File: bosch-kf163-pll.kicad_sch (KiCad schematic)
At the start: 7 parts, among them J101 TGA, U101 ESP32-WROOM-32U

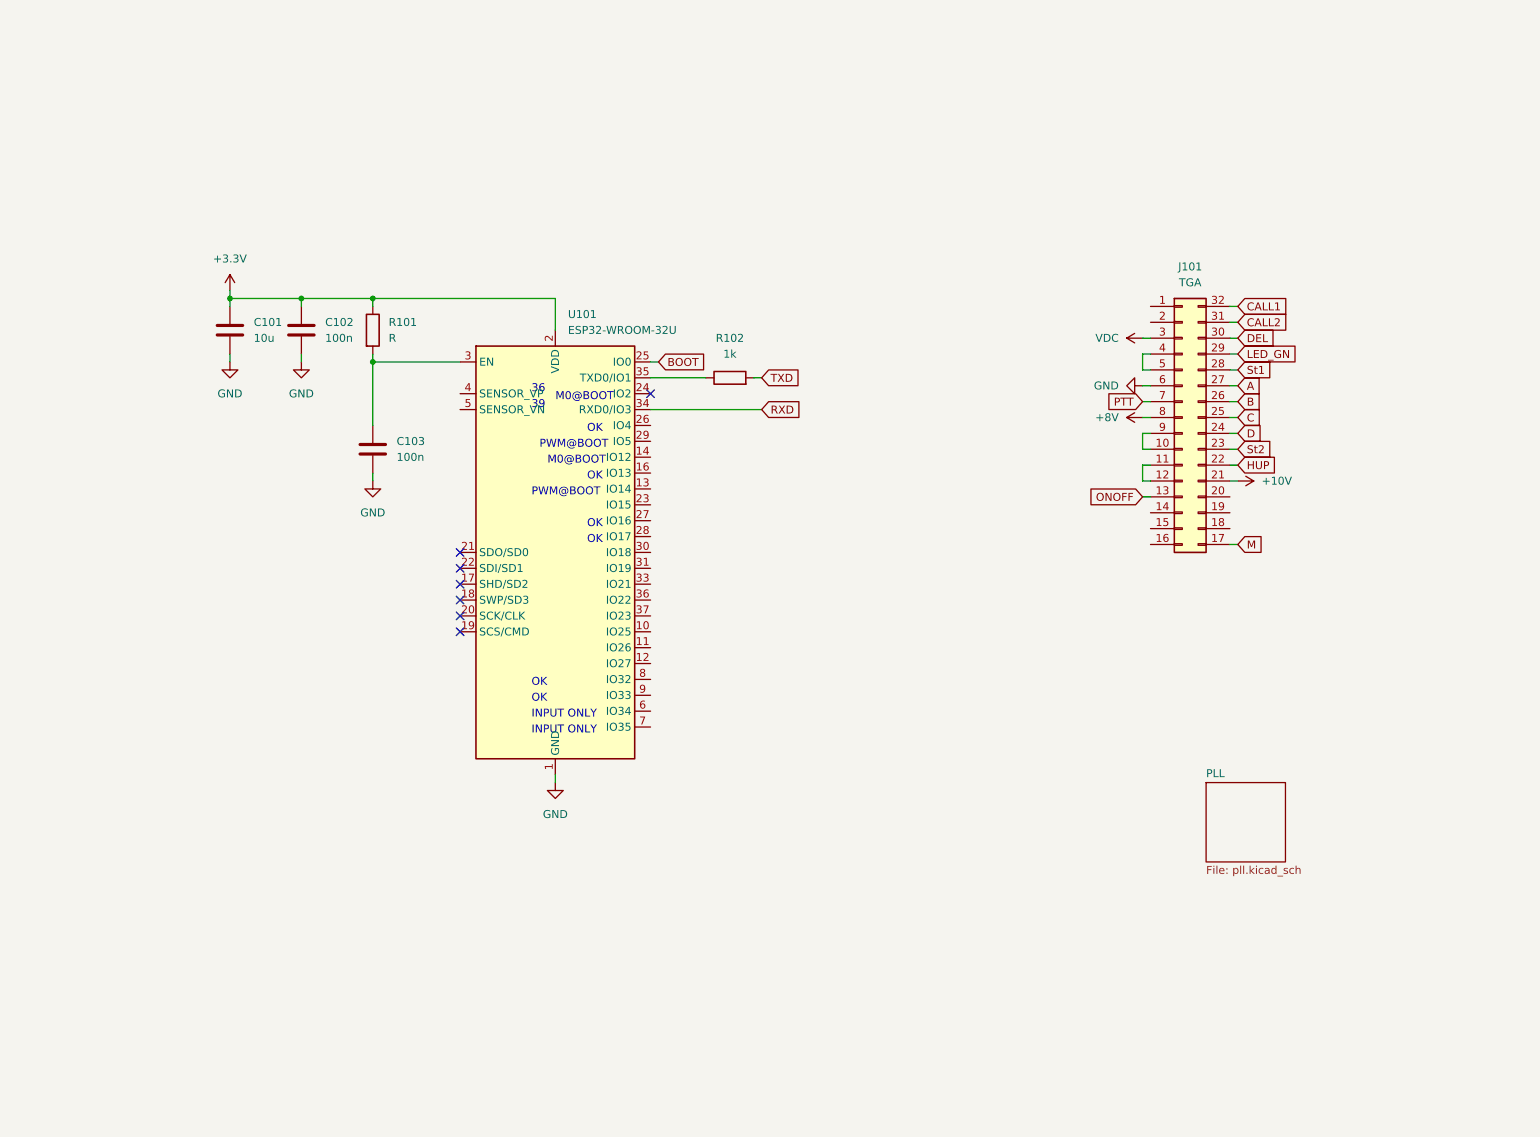
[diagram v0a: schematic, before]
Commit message: Initial TGA-connector, ESP32 and NF-filter circuit.
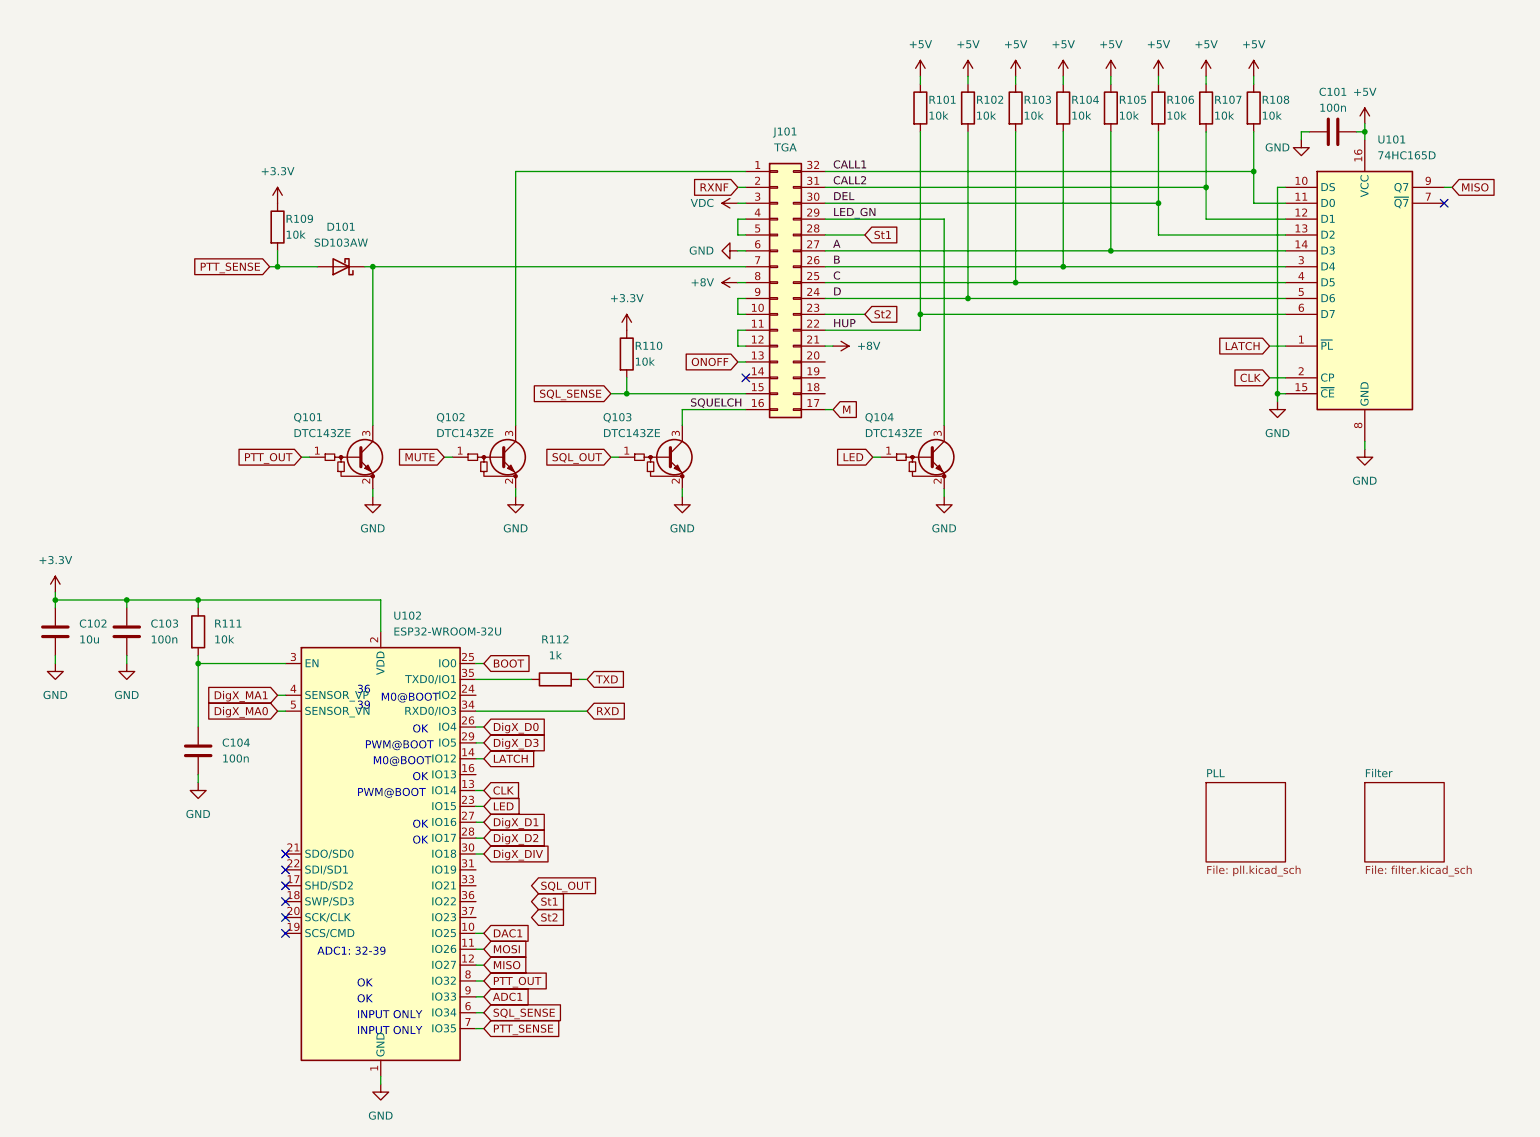
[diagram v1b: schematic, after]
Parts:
- added C101: 100n, Capacitor_SMD:C_0603_1608Metric, symbol Device:C
- added D101: SD103AW, symbol Device:D_Schottky
- added Q101, Q102, Q103, Q104: DTC143ZE, Package_TO_SOT_SMD:SOT-523, symbol Device:Q_NPN_BEC_BRT
- added R101, R102, R103, R104, R105, R106, R107, R108, R109, R110: 10k, symbol Device:R
- added U101: 74HC165D, Package_SO:SO-16_3.9x9.9mm_P1.27mm, symbol 74xx:74HC165
- R111: renamed from R101; value R -> 10k
- renumbered C101 to C102, C102 to C103, C103 to C104, R102 to R112, U101 to U102
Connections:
- net +10V is gone; now on net +8V: J101.21 (Pin_21)
- net +3V3: now also R109.1, R110.1
- net A: now also R105.2, U101.14 (D3)
- net B: now also R104.2, U101.3 (D4)
- net C: now also R103.2, U101.4 (D5)
- net CALL1: now also R108.2, U101.11 (D0)
- net CALL2: now also R107.2, U101.12 (D1)
- net D: now also R102.2, U101.5 (D6)
- net DEL: now also R106.2, U101.13 (D2)
- net GND: now also C101.1, Q101.2 (E), Q102.2 (E), Q103.2 (E), Q104.2 (E), U101.10 (DS), U101.15 (~{CE}), U101.8 (GND)
- net HUP: now also R101.2, U101.6 (D7)
- net LED_GN: now also Q104.3 (C)
- net at J101.1 (Pin_1): now also Q102.3 (C)
- net SQL_SENSE: now reaches J101.15 (Pin_15)
- net SQL_SENSE: now also U102.6 (IO34), R110.2
- net SQUELCH: now reaches J101.16 (Pin_16)
- net SQUELCH: now also Q103.3 (C)
- net RXNF: now reaches J101.2 (Pin_2)
- net DAC1: now reaches U102.10 (IO25)
- net MOSI: now reaches U102.11 (IO26)
- net MISO: now reaches U102.12 (IO27)
- net MISO: now also U101.9 (Q7)
- net CLK: now reaches U102.13 (IO14)
- net CLK: now also U101.2 (CP)
- net LATCH: now reaches U102.14 (IO12)
- net LATCH: now also U101.1 (~{PL})
- net LED: now reaches U102.23 (IO15)
- net LED: now also Q104.1 (B)
- net DigX_D0: now reaches U102.26 (IO4)
- net DigX_D1: now reaches U102.27 (IO16)
- net DigX_D2: now reaches U102.28 (IO17)
- net DigX_D3: now reaches U102.29 (IO5)
- net DigX_DIV: now reaches U102.30 (IO18)
- net DigX_MA1: now reaches U102.4 (SENSOR_VP)
- net DigX_MA0: now reaches U102.5 (SENSOR_VN)
- net PTT_SENSE: now reaches U102.7 (IO35)
- net PTT_SENSE: now also D101.2 (A), R109.2
- net PTT_OUT: now reaches U102.8 (IO32)
- net PTT_OUT: now also Q101.1 (B)
- net ADC1: now reaches U102.9 (IO33)
- net PTT: no longer names the net of J101.7 (Pin_7)
- net PTT: now also D101.1 (K), Q101.3 (C)
- new net +5V: C101.2, R101.1, R102.1, R103.1, R104.1, R105.1, R106.1, R107.1, R108.1, U101.16 (VCC)
- new net MUTE: Q102.1 (B)
- new net SQL_OUT: Q103.1 (B)
- no-connect marks 7 -> 8
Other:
- added sheet Filter (filter.kicad_sch)
- note added: "ADC1: 32-39"
- moved on the sheet: C102, C103, C104, J101, R111, R112, U102

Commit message: schematic/pcb update
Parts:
- removed J101: TGA, symbol Connector_Generic:Conn_02x16_Counter_Clockwise
- added C104, C105: 100n, Capacitor_SMD:C_0603_1608Metric, symbol Device:C
- added D102, D103: SD103AW, Diode_SMD:D_SOD-123, symbol Device:D_Schottky
- added J101: TGA, Connector_PinSocket_2.54mm:PinSocket_2x16_P2.54mm_Vertical, symbol Connector_Generic:Conn_02x16_Odd_Even
- added R109, R110: 4.7k, Resistor_SMD:R_0603_1608Metric, symbol Device:R
- added U102: AMS1117-3.3, Package_TO_SOT_SMD:SOT-223-3_TabPin2, symbol Regulator_Linear:AMS1117-3.3
- D101: footprint (none) -> Diode_SMD:D_SOD-123
- R101, R102, R103, R104, R105, R106, R107, R108: value 10k -> 4.7k; footprint (none) -> Resistor_SMD:R_0603_1608Metric
- R111: renamed from R109; value 10k -> 4.7k; footprint (none) -> Resistor_SMD:R_0603_1608Metric
- R112: renamed from R110; value 10k -> 4.7k; footprint (none) -> Resistor_SMD:R_0603_1608Metric
- R114: renamed from R111; value 10k -> 4.7k
- renumbered C104 to C106, R112 to R113, U102 to U103
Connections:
- net +3V3: now also C101.2, R103.1, R104.1, R105.1, R106.1, R107.1, R108.1, U101.16 (VCC), C105.1, R109.1, R110.1, U102.2 (VO)
- net +8V: now also R101.1, R102.1, C104.1, J101.10 (Pin_10), J101.17 (Pin_17), U102.3 (VI)
- net A: now also R107.2, J101.22 (Pin_22); no longer R105.2
- net B: now also R106.2, J101.20 (Pin_20); no longer R104.2
- net C: now also R105.2, J101.18 (Pin_18); no longer R103.2
- net CALL1: now also J101.32 (Pin_32), R110.2; no longer R108.2
- net CALL2: now also J101.30 (Pin_30), R109.2; no longer R107.2
- net CLK: now also U103.8 (IO32); no longer U103.13 (IO14)
- net D: now also R104.2, J101.16 (Pin_16); no longer R102.2
- net DEL: now also R108.2, J101.28 (Pin_28); no longer R106.2
- net GND: now also C104.2, C105.2, J101.21 (Pin_21), U102.1 (GND); no longer U101.10 (DS)
- net HUP: now also R103.2, J101.12 (Pin_12); no longer R101.2
- net LATCH: now also U103.11 (IO26); no longer U103.14 (IO12)
- net LED: now also U103.36 (IO22); no longer U103.23 (IO15)
- net LED_GN: now also J101.26 (Pin_26)
- net M: now also J101.2 (Pin_2)
- net MISO: now also U103.6 (IO34); no longer U103.12 (IO27)
- net MOSI: now also U103.24 (IO2); no longer U103.11 (IO26)
- net MUTE: now also U103.37 (IO23)
- net ONOFF: now also J101.7 (Pin_7)
- net PTT_OUT: now also U103.12 (IO27); no longer U103.8 (IO32)
- net RXNF: now also J101.29 (Pin_29)
- net SQL_OUT: now also U103.14 (IO12)
- net SQL_SENSE: now also U103.16 (IO13), J101.3 (Pin_3); no longer U103.6 (IO34)
- net SQUELCH: now also J101.1 (Pin_1)
- net St1: now also R101.2, D102.2 (A), J101.24 (Pin_24)
- net St2: now also R102.2, D103.2 (A), J101.14 (Pin_14)
- net TXD: now also U103.35 (TXD0/IO1); no longer R113.2
- net VDC: now also J101.27 (Pin_27)
- net at Q102.3 (C): now also J101.31 (Pin_31)
- net at D101.1 (K), Q101.3 (C): now also J101.19 (Pin_19)
- net at R113.1: now also J101.8 (Pin_8); no longer U103.35 (TXD0/IO1)
- net at U103.31 (IO19): now also D103.1 (K)
- removed net +5V: C101.2, R101.1, R102.1, R103.1, R104.1, R105.1, R106.1, R107.1, R108.1, U101.16 (VCC)
- new net: D102.1 (K), U103.13 (IO14)
- new net: J101.11 (Pin_11), J101.9 (Pin_9)
- new net: J101.13 (Pin_13), J101.15 (Pin_15)
- new net: J101.23 (Pin_23), J101.25 (Pin_25)
- new net MISO_PLL: U101.10 (DS)
- no-connect marks 8 -> 19
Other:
- moved on the sheet: C101, D101, Q101, Q102, Q103, Q104, R111, R112, R113, U101

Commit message: schematic/pcb update
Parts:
- added J102: PROG, Connector_PinHeader_2.54mm:PinHeader_1x04_P2.54mm_Horizontal, symbol Connector:Conn_01x04_Male
- added R115, R116, R117: 0, Resistor_SMD:R_0603_1608Metric, symbol Device:R
- J101: LCSC (none) -> C115248
- U101: footprint Package_SO:SO-16_3.9x9.9mm_P1.27mm -> Package_SO:SOIC-16_3.9x9.9mm_P1.27mm
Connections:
- net M is gone; now on net SQUELCH: J101.2 (Pin_2)
- net +8V: now also J101.18 (Pin_18), J101.9 (Pin_9); no longer J101.10 (Pin_10), J101.17 (Pin_17)
- net A: now also J101.21 (Pin_21); no longer J101.22 (Pin_22)
- net B: now also J101.19 (Pin_19); no longer J101.20 (Pin_20)
- net BOOT: now also J102.2 (Pin_2), R115.2
- net C: now also J101.17 (Pin_17); no longer J101.18 (Pin_18)
- net CALL1: now also J101.31 (Pin_31); no longer J101.32 (Pin_32)
- net CALL2: now also J101.29 (Pin_29); no longer J101.30 (Pin_30)
- net D: now also J101.15 (Pin_15); no longer J101.16 (Pin_16)
- net DEL: now also J101.27 (Pin_27); no longer J101.28 (Pin_28)
- net GND: now also J101.22 (Pin_22), J102.1 (Pin_1); no longer J101.21 (Pin_21)
- net HUP: now also J101.11 (Pin_11); no longer J101.12 (Pin_12)
- net LED_GN: now also J101.25 (Pin_25); no longer J101.26 (Pin_26)
- net ONOFF: now also J101.8 (Pin_8); no longer J101.7 (Pin_7)
- net RXD: now also J102.3 (Pin_3), R116.2
- net RXNF: now also J101.30 (Pin_30); no longer J101.29 (Pin_29)
- net SQL_SENSE: now also J101.4 (Pin_4); no longer J101.3 (Pin_3)
- net SQUELCH: no longer J101.1 (Pin_1)
- net St1: now also J101.23 (Pin_23); no longer J101.24 (Pin_24)
- net St2: now also J101.13 (Pin_13); no longer J101.14 (Pin_14)
- net TXD: now also R113.2, J102.4 (Pin_4), R117.2; no longer U103.35 (TXD0/IO1)
- net VDC: now also J101.28 (Pin_28); no longer J101.27 (Pin_27)
- net at D101.1 (K), Q101.3 (C): now also J101.20 (Pin_20); no longer J101.19 (Pin_19)
- net at R113.1: now also U103.35 (TXD0/IO1); no longer J101.8 (Pin_8)
- net at Q102.3 (C): now also J101.32 (Pin_32); no longer J101.31 (Pin_31)
- net at J101.5 (Pin_5): now also R116.1
- new net: J101.7 (Pin_7), R115.1
- new net: J101.3 (Pin_3), R117.1
- new net MIC: J101.1 (Pin_1)
- new net RX_FLAT: J101.14 (Pin_14), J101.16 (Pin_16)
- new net TX_FLAT: J101.10 (Pin_10), J101.12 (Pin_12)
- new net TX_NF: J101.24 (Pin_24), J101.26 (Pin_26)
- no-connect marks 19 -> 12
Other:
- note added: "Only place for external UART control without Hbt or Btm control head. Hbt/Btm connect this lines to +8V !"
- moved on the sheet: D102, D103, J101, Q104, R113

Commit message: schematic/pcb update
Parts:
- C104, C105: value 100n -> 10u
- U102: LCSC (none) -> C173386
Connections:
- net RXD: now also R117.2; no longer R116.2
- net TXD: now also R116.2; no longer R117.2
- net RXNF renamed RX_NF
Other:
- moved on the sheet: J102

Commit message: Finished schematic (BOM consolidation, LCSC part numbers) + sheet comments
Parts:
- C101, C103, C106: LCSC (none) -> C14663
- C102, C104, C105: LCSC (none) -> C2922482
- R101, R102, R103, R104, R105, R106, R107, R108, R109, R110, R111, R112, R114: LCSC (none) -> C105428
- R113: value 1k -> 0; LCSC (none) -> C100044
- U103: LCSC (none) -> C328062
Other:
- company: (none) -> Robin Olejnik
- title: (none) -> Bosch KF163 control
